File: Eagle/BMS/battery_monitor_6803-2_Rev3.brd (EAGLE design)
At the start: 88.1 x 53.3 mm, 65 parts, among them Q1 MOSFET-PCHANNELIRLML2244, Q10 IRF9530, Q2 MOSFET-NCHANNELBSS138, Q3 MOSFET-PCHANNELIRLML2244, Q4 MOSFET-PCHANNELIRLML2244, Q5 MOSFET-PCHANNELIRLML2244, Q6 MOSFET-NCHANNELBSS138, Q7 MOSFET-NCHANNELBSS138, Q8 MOSFET-NCHANNELBSS138, Q9 PMOS_AO4435

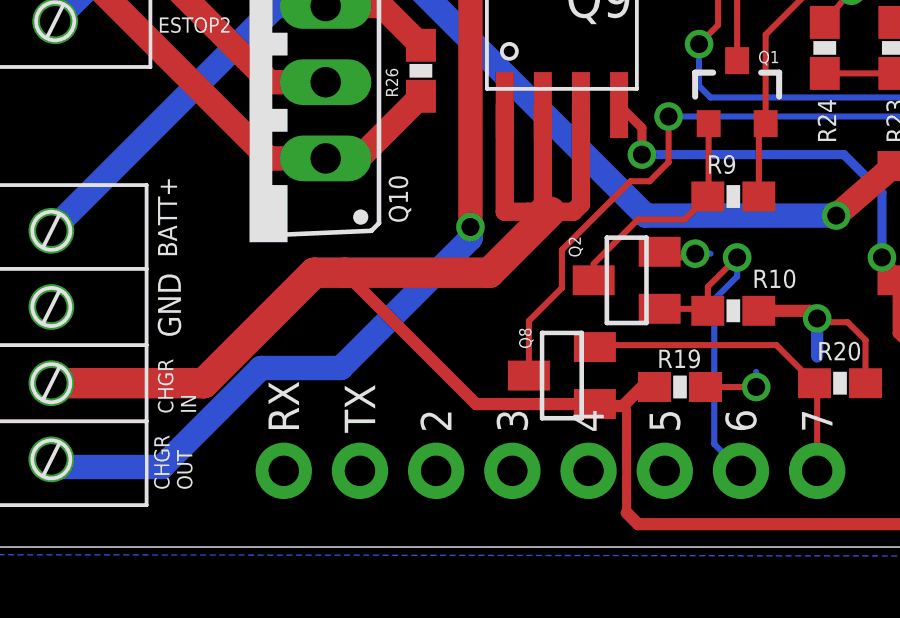
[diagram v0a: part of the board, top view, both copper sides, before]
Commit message: Fixed error with charging line shorting to +5V
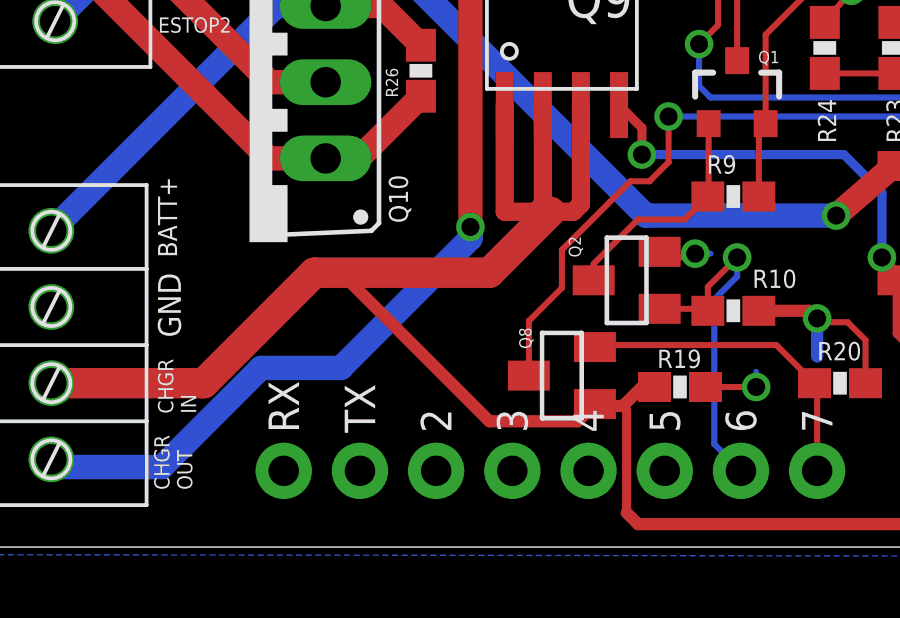
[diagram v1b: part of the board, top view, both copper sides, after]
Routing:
- net CHARGER_IN: track 64.2 -> 65.7 mm
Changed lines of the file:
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@@
 <wire x1="21.336" y1="15.494" x2="21.336" y2="12.192" width="0.6096" layer="1"/>
 <wire x1="21.336" y1="12.192" x2="21.082" y2="11.938" width="0.6096" layer="1"/>
-<wire x1="21.082" y1="11.938" x2="20.828" y2="11.938" width="0.6096" layer="1"/>
-<wire x1="20.828" y1="11.938" x2="20.066" y2="11.938" width="0.6096" layer="1"/>
+<wire x1="21.082" y1="11.938" x2="20.066" y2="11.938" width="0.6096" layer="1"/>
 <wire x1="22.606" y1="15.494" x2="22.606" y2="12.192" width="0.6096" layer="1"/>
 <wire x1="22.606" y1="12.192" x2="22.352" y2="11.938" width="0.6096" layer="1"/>
 <wire x1="22.352" y1="11.938" x2="21.59" y2="11.938" width="0.6096" layer="1"/>
-<wire x1="13.716" y1="9.906" x2="14.732" y2="9.906" width="1.016" layer="1"/>
-<wire x1="23.071" y1="5.527" x2="19.111" y2="5.527" width="0.4064" layer="1"/>
-<wire x1="19.111" y1="5.527" x2="14.732" y2="9.906" width="0.4064" layer="1"/>
 <wire x1="13.716" y1="9.906" x2="10.033" y2="6.223" width="1.016" layer="1"/>
 <wire x1="10.033" y1="6.223" x2="4.953" y2="6.223" width="1.016" layer="1"/>
-<wire x1="14.732" y1="9.906" x2="19.558" y2="9.906" width="1.016" layer="1"/>
+<wire x1="13.716" y1="9.906" x2="19.558" y2="9.906" width="1.016" layer="1"/>
 <wire x1="19.558" y1="9.906" x2="21.59" y2="11.938" width="1.016" layer="1"/>
 <wire x1="21.59" y1="11.938" x2="21.082" y2="11.938" width="0.6096" layer="1"/>
+<wire x1="13.716" y1="9.906" x2="14.605" y2="9.906" width="0.4064" layer="1"/>
+<wire x1="14.605" y1="9.906" x2="19.558" y2="4.953" width="0.4064" layer="1"/>
+<wire x1="19.558" y1="4.953" x2="22.497" y2="4.953" width="0.4064" layer="1"/>
+<wire x1="22.497" y1="4.953" x2="23.071" y2="5.527" width="0.4064" layer="1"/>
 </signal>
 <signal name="GPIO2">
